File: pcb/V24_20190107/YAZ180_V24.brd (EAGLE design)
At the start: 160 x 100 mm, 117 parts, among them IC1 74LS93D, IC10 LM2674AM-12V, IC11 FT232RL, IC12 FT245RL, IC13 74HCT04D, IC14 PCA9665, IC15 PCA9665, IC17 LM2596S-5V, IC3 74ACT74D, IC4 IS62WV10248DALL-55T, IC5 SST39VF010, IC6 ATF16V8BP3, IC7 ATF16V8BP3, IC8 74121D, IC9 82c55, J1 DC-005, J2 I2C Grove 2, J3 I2C Grove 1, J6 I2C Pinout 1, J7 I2C Pinout 2, SW1 SINGLE STEP, SW2 RESET, SW3 DIP-SLIDE-SWITCH(3P-11.6X4.0X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, U1 Z8X180PLCC68-S, U2 AM9511A-1, U21 MAX6817EUT+T, U22 TLC7705ID, U3 SN74ABTH245DW, U4 SN74ABT541BDW, U5 CJ1117-3.3-1310120P1, U7 SN74LVC1G97DCKR, X1 ASCI0 - USB, X2 USB Programmer, X3 FIDUCIAL_0.6-1.2MM, X4 FIDUCIAL_0.6-1.2MM, X5 FIDUCIAL_0.6-1.2MM, X6 FIDUCIAL_0.6-1.2MM, Y1 18.432MHZ

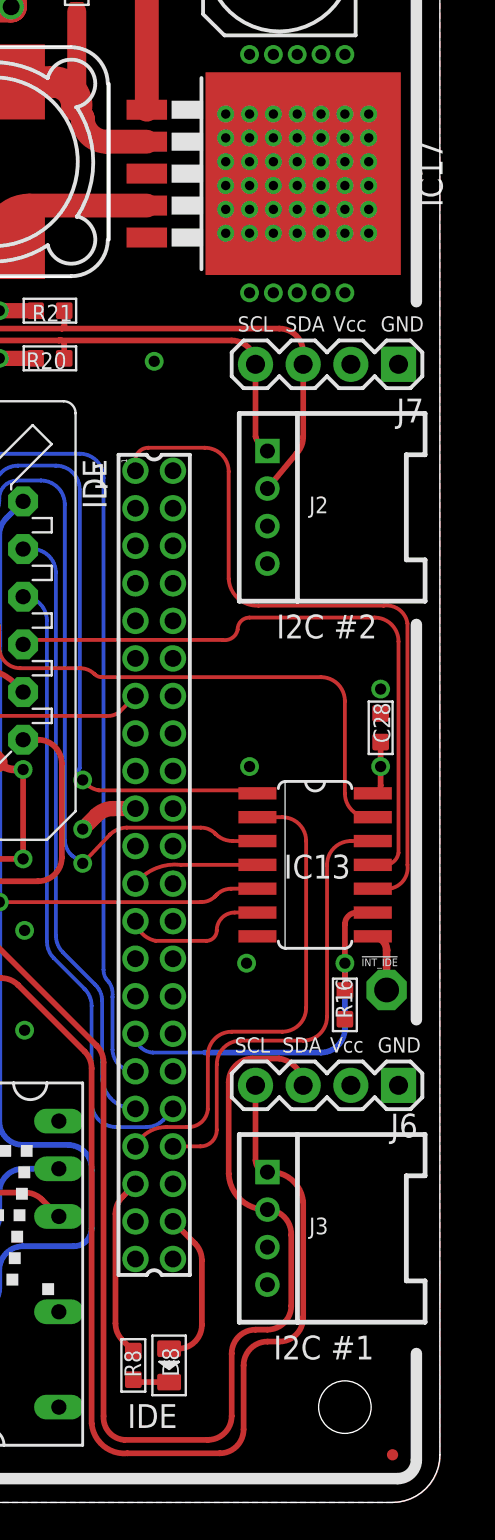
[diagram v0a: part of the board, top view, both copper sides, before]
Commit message: PCB - delete names from silk
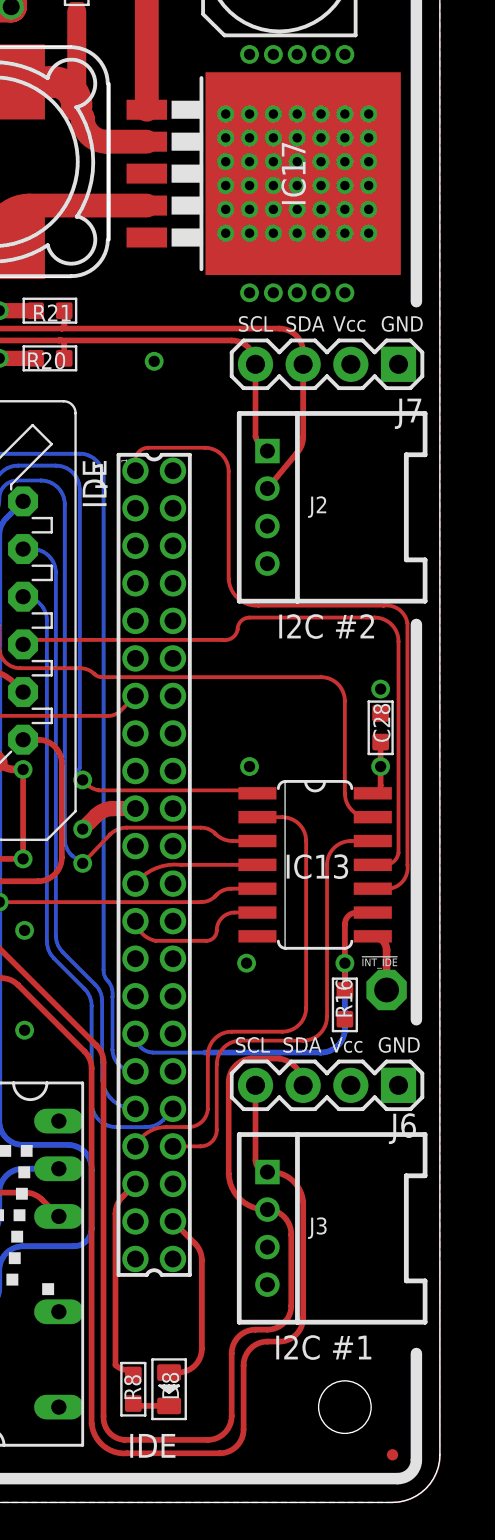
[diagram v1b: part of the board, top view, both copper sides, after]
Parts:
- moved D8 1.27 mm to (145.6, 6.03)
- moved R8 1.27 mm to (143.7, 6.03)
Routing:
- net !ACT: track 9.58 -> 11.1 mm
- net VCC: track 863.3 -> 864.6 mm
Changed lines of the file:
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@@
 <rectangle x1="58.1025" y1="39.6875" x2="66.04" y2="45.4025" layer="41"/>
 <rectangle x1="89.2175" y1="61.595" x2="93.0275" y2="70.485" layer="41"/>
-<text x="143.35125" y="3.96875" size="1.27" layer="21" ratio="11">IDE</text>
+<text x="143.35125" y="2.38125" size="1.27" layer="21" ratio="11">IDE</text>
 <wire x1="158.75" y1="25.7175" x2="158.75" y2="46.78375" width="0.6096" layer="21"/>
 <text x="141.44625" y="54.054375" size="1.27" layer="21" ratio="11">1</text>
@@
 <attribute name="MF" value="NATIONAL SEMICONDUCTOR" x="150.1775" y="70.8025" size="1.778" layer="27" rot="R270" display="off"/>
 <attribute name="OC_FARNELL" value="9494367" x="150.1775" y="70.8025" size="1.778" layer="27" rot="R270" display="off"/>
-<attribute name="NAME" x="160.147" y="69.0245" size="1.27" layer="25" rot="R90"/>
+<attribute name="NAME" x="152.8445" y="69.0245" size="1.27" layer="25" rot="R90"/>
 <attribute name="VALUE" x="146.4945" y="63.627" size="1.27" layer="27"/>
 </element>
@@
 <attribute name="NAME" x="126.0475" y="89.916" size="0.635" layer="33" ratio="10"/>
 </element>
-<element name="R8" library="Seeed-OPL-Resistor" package="R0603" value="270R" x="143.66875" y="7.3025" smashed="yes">
-<attribute name="MPN" value="RC0603FR-07270RL" x="140.17625" y="11.43" size="1.778" layer="27" display="off"/>
-<attribute name="NAME" x="144.0815" y="6.6675" size="0.889" layer="25" ratio="11" rot="R90"/>
-<attribute name="VALUE" x="144.145" y="6.19125" size="0.635" layer="27" ratio="10" rot="R90"/>
-</element>
-<element name="D8" library="Seeed-OPL-Diode" package="LED-0805" value="SMD-LED-CLEAR-RED(0805)" x="145.57375" y="7.3025" smashed="yes" rot="R270">
-<attribute name="MPN" value="17-215SURC/S530-A2/TR8" x="149.38375" y="10.795" size="1.778" layer="27" rot="R270" display="off"/>
-<attribute name="NAME" x="145.208625" y="8.255" size="0.889" layer="25" font="vector" ratio="11" rot="R270"/>
-<attribute name="VALUE" x="147.6375" y="3.762375" size="0.635" layer="27" ratio="10" rot="R90"/>
+<element name="R8" library="Seeed-OPL-Resistor" package="R0603" value="270R" x="143.66875" y="6.0325" smashed="yes">
+<attribute name="MPN" value="RC0603FR-07270RL" x="140.17625" y="10.16" size="1.778" layer="27" display="off"/>
+<attribute name="NAME" x="144.0815" y="5.3975" size="0.889" layer="25" ratio="11" rot="R90"/>
+<attribute name="VALUE" x="144.145" y="4.92125" size="0.635" layer="27" ratio="10" rot="R90"/>
+</element>
+<element name="D8" library="Seeed-OPL-Diode" package="LED-0805" value="SMD-LED-CLEAR-RED(0805)" x="145.57375" y="6.0325" smashed="yes" rot="R270">
+<attribute name="MPN" value="17-215SURC/S530-A2/TR8" x="149.38375" y="9.525" size="1.778" layer="27" rot="R270" display="off"/>
+<attribute name="NAME" x="145.208625" y="6.985" size="0.889" layer="25" font="vector" ratio="11" rot="R270"/>
+<attribute name="VALUE" x="147.6375" y="2.492375" size="0.635" layer="27" ratio="10" rot="R90"/>
 </element>
 <element name="R16" library="Seeed-OPL-Resistor-V2" package="R0603" value="10K" x="154.94" y="26.51125" smashed="yes" rot="R180">
@@
 <wire x1="86.6775" y1="76.835" x2="87.63" y2="77.7875" width="0.3048" layer="1" curve="90"/>
 <wire x1="87.63" y1="77.7875" x2="87.63" y2="78.4225" width="0.3048" layer="1"/>
-<wire x1="147.32" y1="12.90875" x2="147.32" y2="9.4615" width="0.3048" layer="1"/>
-<wire x1="147.32" y1="9.4615" x2="146.05" y2="8.1915" width="0.3048" layer="1" curve="-90"/>
-<wire x1="146.05" y1="8.1915" x2="145.57375" y2="8.1915" width="0.3048" layer="1"/>
+<wire x1="147.32" y1="12.90875" x2="147.32" y2="8.1915" width="0.3048" layer="1"/>
+<wire x1="147.32" y1="8.1915" x2="146.05" y2="6.9215" width="0.3048" layer="1" curve="-90"/>
+<wire x1="146.05" y1="6.9215" x2="145.57375" y2="6.9215" width="0.3048" layer="1"/>
 </signal>
 <signal name="ADDR0">
@@
 <contactref element="R8" pad="2"/>
 <contactref element="D8" pad="-"/>
-<wire x1="143.66875" y1="6.5405" x2="143.79575" y2="6.4135" width="0.3048" layer="1" curve="90"/>
-<wire x1="143.79575" y1="6.4135" x2="145.57375" y2="6.4135" width="0.3048" layer="1"/>
+<wire x1="143.66875" y1="5.2705" x2="143.79575" y2="5.1435" width="0.3048" layer="1" curve="90"/>
+<wire x1="143.79575" y1="5.1435" x2="145.57375" y2="5.1435" width="0.3048" layer="1"/>
 </signal>
 <signal name="!ACT">
@@
 <wire x1="142.71625" y1="15.3827" x2="143.088225" y2="16.280725" width="0.3048" layer="1" curve="-45"/>
 <wire x1="143.088225" y1="16.280725" x2="143.78" y2="16.9725" width="0.3048" layer="1"/>
-<wire x1="142.71625" y1="15.3827" x2="142.71625" y2="9.54305" width="0.3048" layer="1"/>
-<wire x1="142.71625" y1="9.54305" x2="143.088225" y2="8.645025" width="0.3048" layer="1" curve="45"/>
-<wire x1="143.088225" y1="8.645025" x2="143.66875" y2="8.0645" width="0.3048" layer="1"/>
+<wire x1="142.71625" y1="15.3827" x2="142.71625" y2="7.32055" width="0.3048" layer="1"/>
+<wire x1="142.71625" y1="7.32055" x2="143.405725" y2="7.057525" width="0.3048" layer="1" curve="45"/>
+<wire x1="143.405725" y1="7.057525" x2="143.66875" y2="6.7945" width="0.3048" layer="1"/>
 </signal>
 <signal name="PA0">
